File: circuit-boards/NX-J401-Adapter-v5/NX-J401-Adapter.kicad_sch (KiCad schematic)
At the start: 20 parts, among them J1 V_OUT, J2 NX BUTTON, J3 Power, SW1 RECOVERY, SW2 RESET

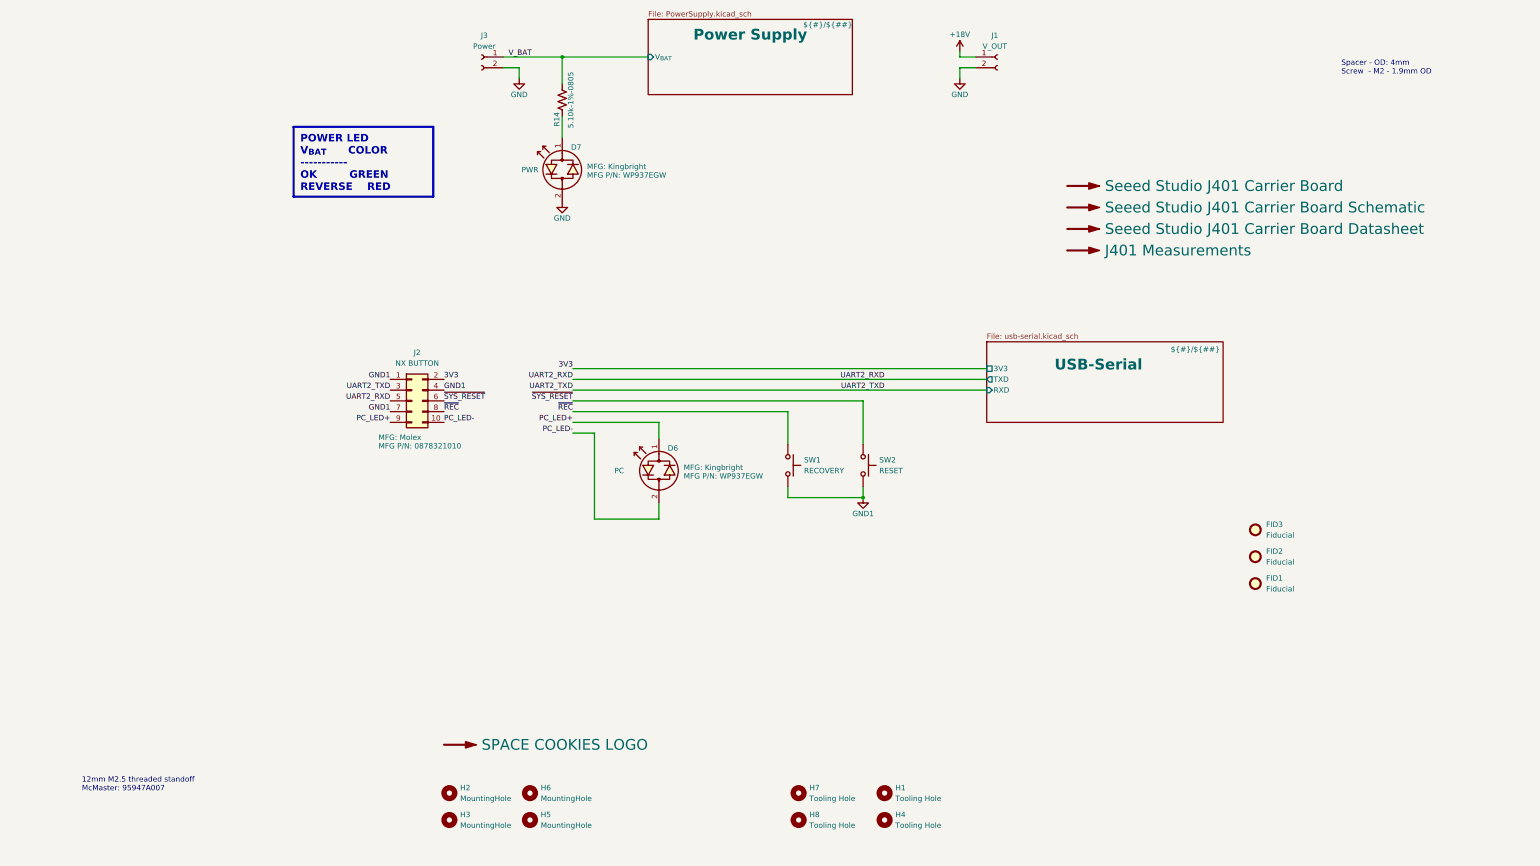
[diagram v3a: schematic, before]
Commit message: Update NX J401 to combine button interface and adapter. change header to right angle
Signed-off-by: Scott Berman <sgberman1@gmail.com>
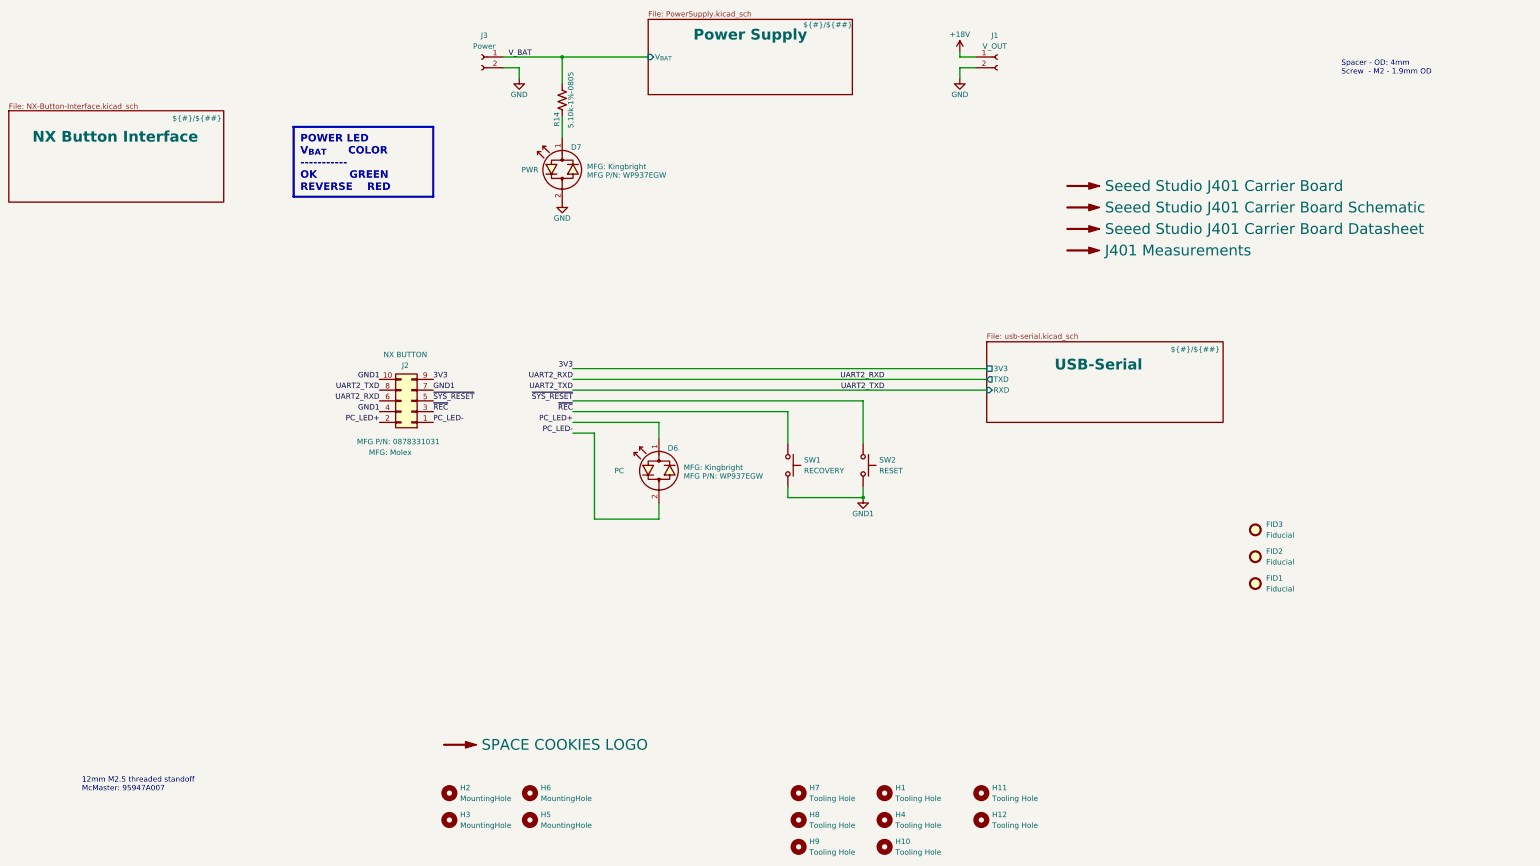
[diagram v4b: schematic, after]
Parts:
- added H10, H11, H12, H9: Tooling Hole, MountingHole:ToolingHole_1.152mm, symbol Mechanical:MountingHole
- J2: footprint NX-J401-Adapter:Molex-878321010 -> NX-J401-Adapter:Molex-0878331031; DIST P/N WM4227-ND -> WM3598-ND; MFG P/N 0878321010 -> 0878331031
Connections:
- net 3V3: now also J2.9 (Pin_9); no longer J2.2 (Pin_2)
- net GND1: now also J2.10 (Pin_10); no longer J2.1 (Pin_1)
- net PC_LED+: now also J2.2 (Pin_2); no longer J2.9 (Pin_9)
- net PC_LED-: now also J2.1 (Pin_1); no longer J2.10 (Pin_10)
- net UART2_RXD: now also J2.6 (Pin_6); no longer J2.5 (Pin_5)
- net UART2_TXD: now also J2.8 (Pin_8); no longer J2.3 (Pin_3)
- net ~{REC}: now also J2.3 (Pin_3); no longer J2.8 (Pin_8)
- net ~{SYS_RESET}: now also J2.5 (Pin_5); no longer J2.6 (Pin_6)
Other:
- added sheet NX Button Interface (NX-Button-Interface.kicad_sch)
- moved on the sheet: J2

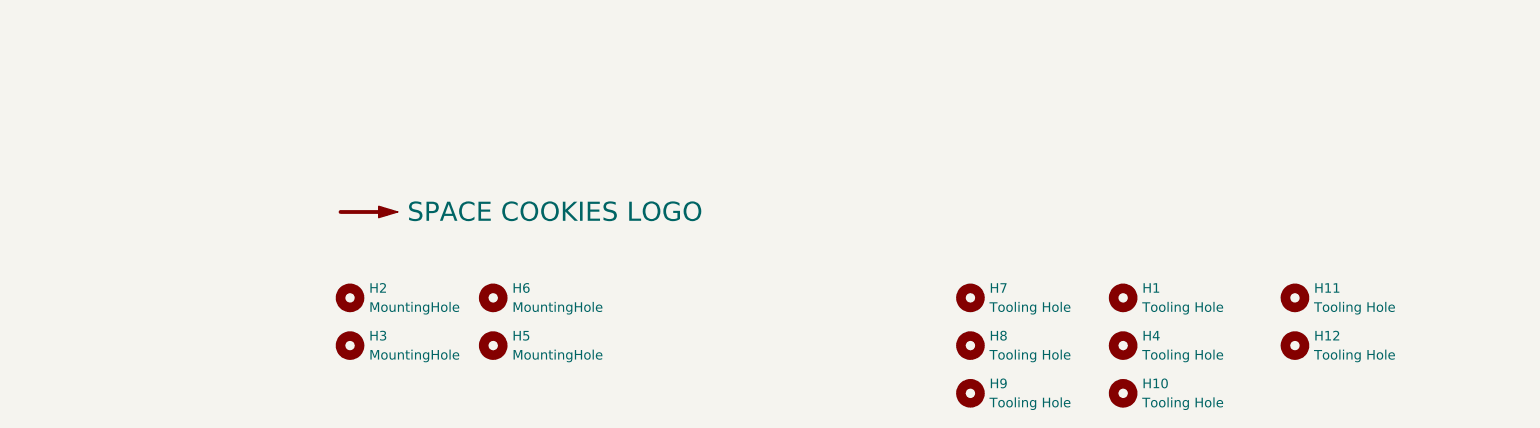
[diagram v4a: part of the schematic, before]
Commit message: Fix bom to reduce line items. Addd zip tie slots. Add 1.5mm tooling holes
Signed-off-by: Scott Berman <sgberman1@gmail.com>
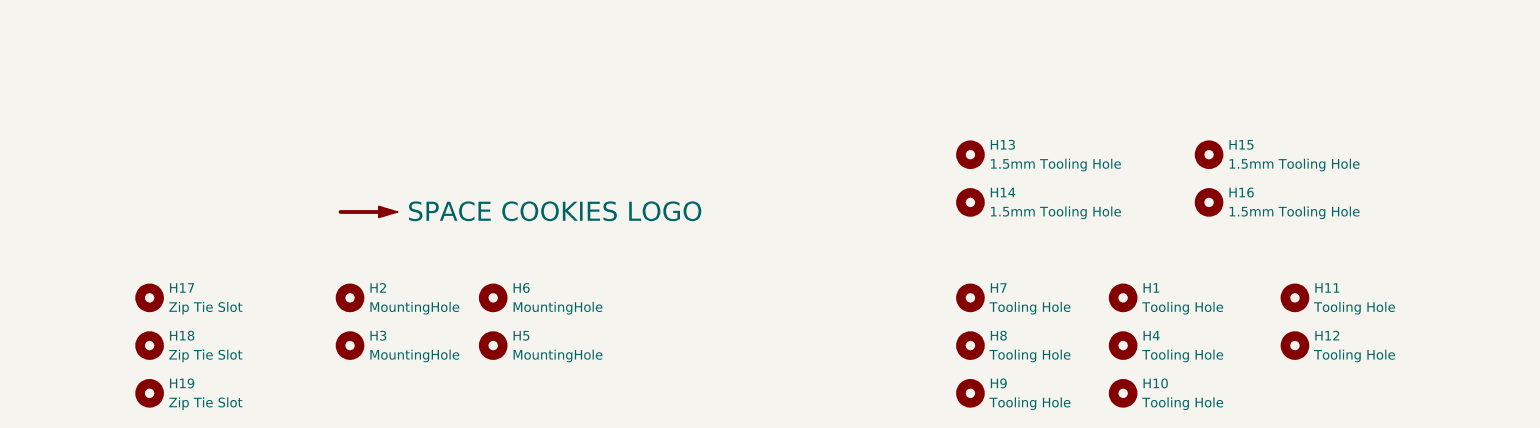
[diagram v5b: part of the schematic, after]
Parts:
- added H13, H14, H15, H16: 1.5mm Tooling Hole, NX-J401-Adapter:ToolingHole_1.5mm, symbol Mechanical:MountingHole
- added H17, H18, H19: Zip Tie Slot, NX-J401-Adapter:Zip-tie-slot, symbol Mechanical:MountingHole

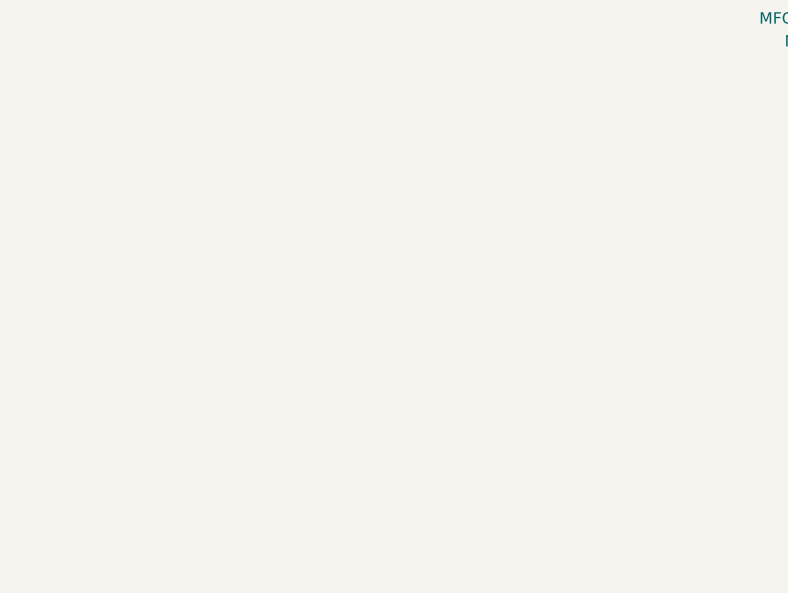
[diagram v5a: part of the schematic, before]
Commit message: Add ribbon cable connector and cable to schematic
Signed-off-by: Scott Berman <scott.berman@bluerivertech.com>
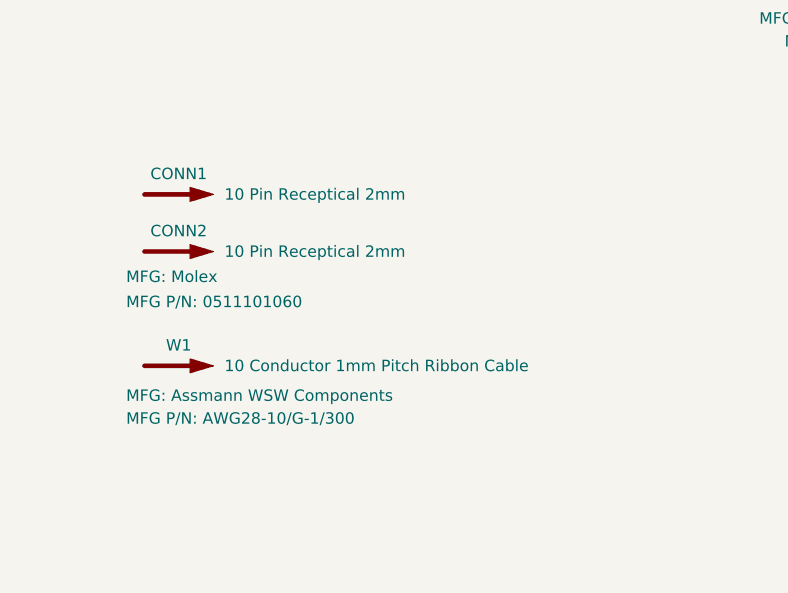
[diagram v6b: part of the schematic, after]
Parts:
- added CONN1, CONN2: 10 Pin Receptical 2mm, symbol Graphic:SYM_Arrow_Large
- added W1: 10 Conductor 1mm Pitch Ribbon Cable, symbol Graphic:SYM_Arrow_Large

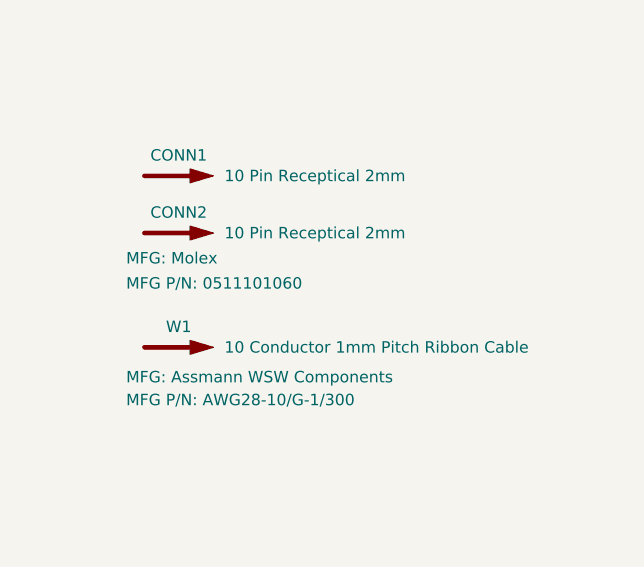
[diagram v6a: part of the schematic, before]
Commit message: Fixed IDC connector part number
Signed-off-by: Scott Berman <scott.berman@bluerivertech.com>
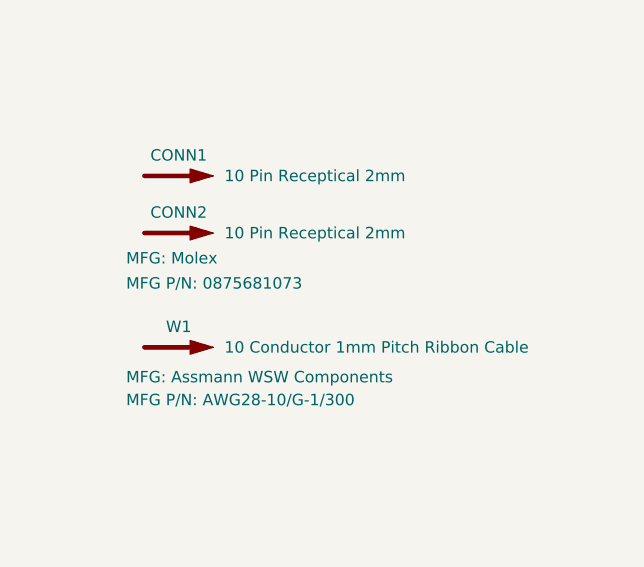
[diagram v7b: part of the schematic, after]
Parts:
- CONN1, CONN2: DIST Digikey -> Mouser; DIST P/N WM3341-ND -> 538-87568-1073; MFG P/N 0511101060 -> 0875681073
- R14: DIST P/N 311-5.10KCRCT-ND -> 13-RC0805FR-135K1LCT-ND; MFG P/N RC0805FR-075K1L -> RC0805FR-135K1L
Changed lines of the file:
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@@
 			)
 		)
-		(property "MFG P/N" "RC0805FR-075K1L"
+		(property "MFG P/N" "RC0805FR-135K1L"
 			(at 161.29 83.82 0)
 			(effects
@@
 			)
 		)
-		(property "DIST P/N" "311-5.10KCRCT-ND"
+		(property "DIST P/N" "13-RC0805FR-135K1LCT-ND"
 			(at 161.29 83.82 0)
 			(effects
@@
 			)
 		)
-		(property "MFG P/N" "0511101060"
+		(property "MFG P/N" "0875681073"
 			(at 42.418 196.088 0)
 			(show_name yes)
@@
 			)
 		)
-		(property "DIST" "Digikey"
+		(property "DIST" "Mouser"
 			(at 48.26 184.15 0)
 			(effects
@@
 			)
 		)
-		(property "DIST P/N" "WM3341-ND"
+		(property "DIST P/N" "538-87568-1073"
 			(at 48.26 184.15 0)
 			(effects
@@
 			)
 		)
-		(property "MFG P/N" "0511101060"
+		(property "MFG P/N" "0875681073"
 			(at 48.26 190.5 0)
 			(effects
@@
 			)
 		)
-		(property "DIST" "Digikey"
+		(property "DIST" "Mouser"
 			(at 48.26 190.5 0)
 			(effects
@@
 			)
 		)
-		(property "DIST P/N" "WM3341-ND"
+		(property "DIST P/N" "538-87568-1073"
 			(at 48.26 190.5 0)
 			(effects
